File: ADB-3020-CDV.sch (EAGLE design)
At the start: 118 parts, among them IC1 7812T, IC2 NE5532N, IC3 LM2576, IC4 NE555, IC5 IR2184D, J1 + IN, J2 - IN, J3 - IN, J4 - OUT, J5 PIN2F061.040, J6 + OUT, J7 PIN2F061.040, J8 + IN, Q1 IRFP240-H, Q2 IRFP240-H, Q4 BDX53, T1 BC337, T2 BC337, X1-1 LSP13, X1-2 LSP13, X2-1 LSP13, X2-2 LSP13

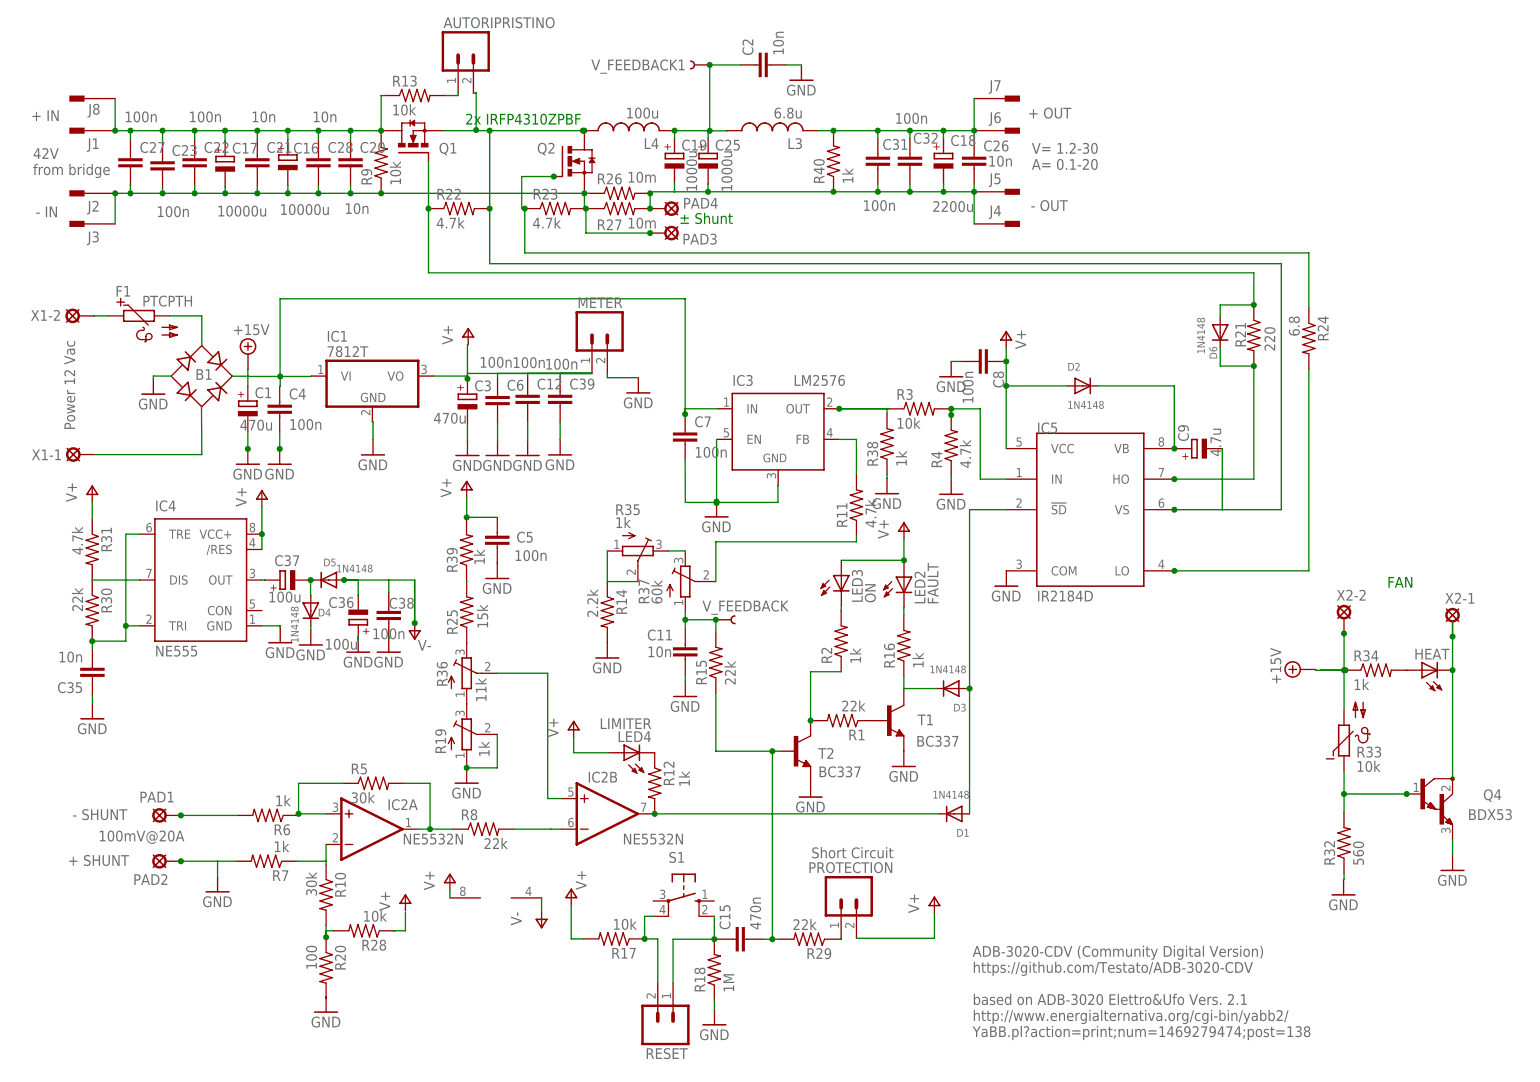
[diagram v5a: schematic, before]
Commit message: Grid 0,1" + some component name corrections
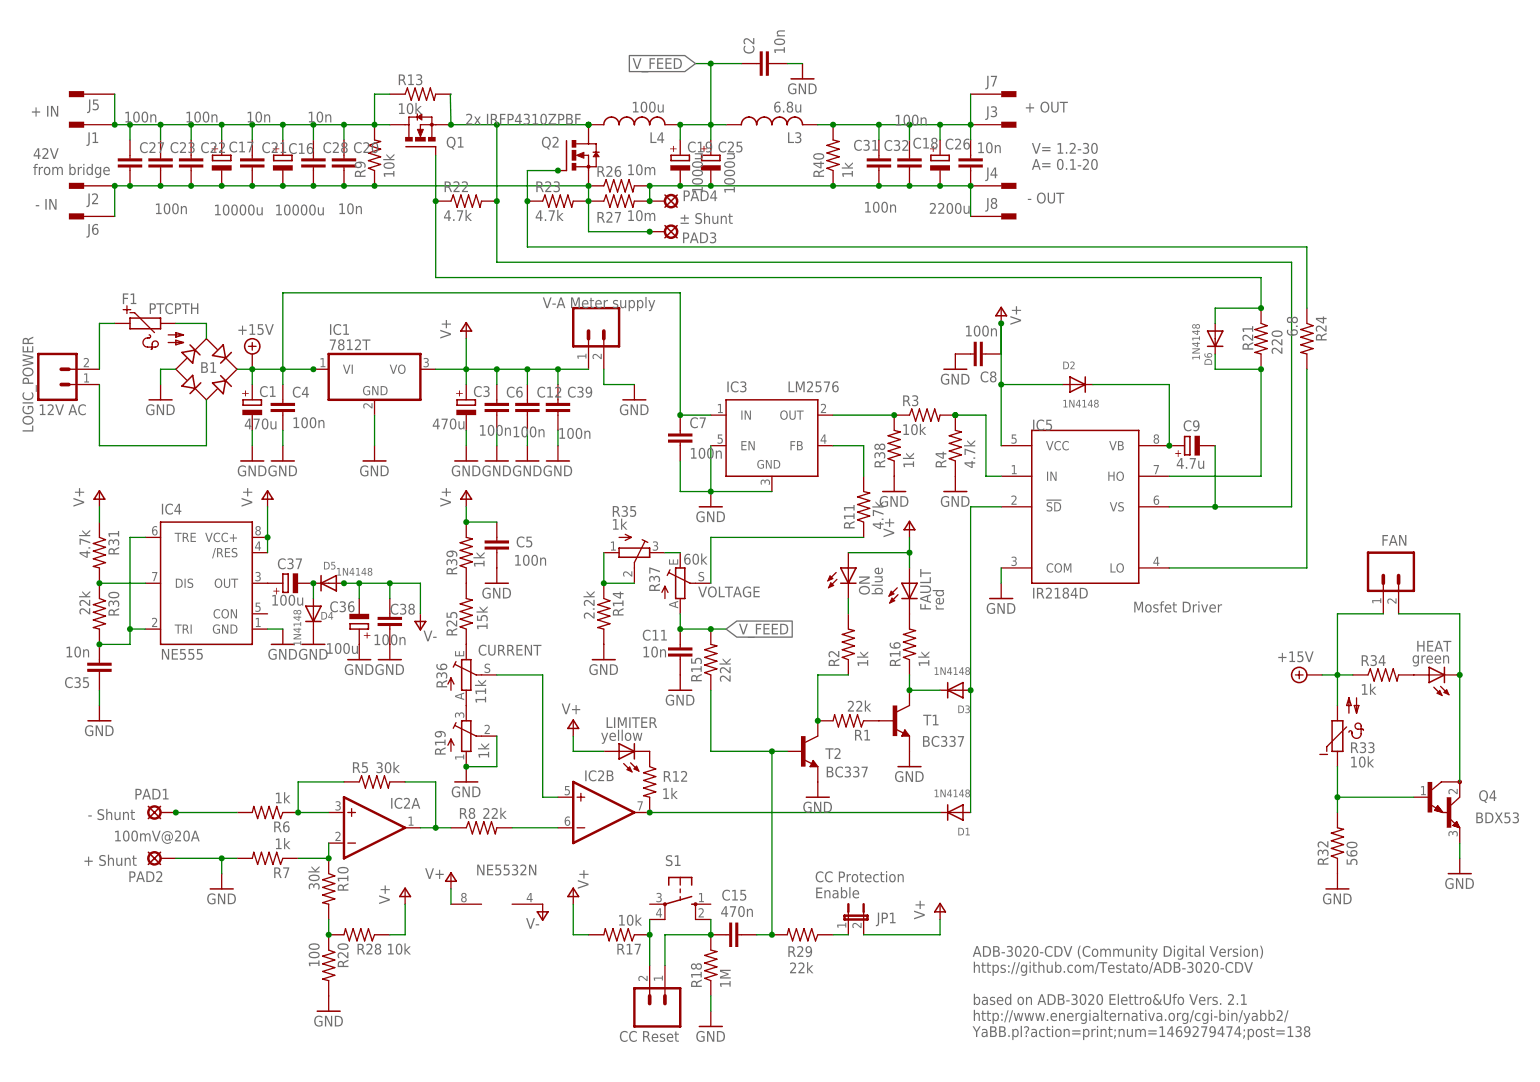
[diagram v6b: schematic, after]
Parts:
- removed AUTORIPRISTINO, METER: (no value), con-amp-quick:MA02
- removed LED2: FAULT, adafruit:LED3MM
- removed LED3: ON, adafruit:LED3MM
- removed LED4: LIMITER, adafruit:LED3MM
- removed PROTECTION: Short Circuit, con-amp-quick:MA02
- removed V_FEEDBACK, V_FEEDBACK1: MPB1, con-hirschmann:MPB1
- removed X1-1, X1-2, X2-1, X2-2: LSP13, solpad:LSP13
- added FAN: fan, con-amp-quick:MA02
- added FAULT: red, adafruit:LED3MM
- added JP1: jp1, jumper:JP1E
- added LIMITER: yellow, adafruit:LED3MM
- added LOGIC_POWER: 12V AC, con-amp-quick:MA02
- added ON: blue, adafruit:LED3MM
- added V-A_METER_SUPPLY: V-A Meter supply, con-amp-quick:MA02
- HEAT: value (none) -> green
- J3: value - IN -> + OUT
- J4: value - OUT -> PIN2F061.040
- J5: value PIN2F061.040 -> + IN
- J6: value + OUT -> - IN
- J8: value + IN -> - OUT
- R36, R37: device adafruit:TRIMPOT3386 -> pot:TRIM_1234-S64YW
- RESET, S1: value (none) -> CC Reset
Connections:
- removed net N$11: C19.+, C25.+, L4.2
- removed net N$13: PROTECTION.1, R29.1
- removed net N$16: C7.1, IC3.IN
- removed net N$17: C7.2
- removed net N$33: IC2B.-IN
- removed net N$38: R8.2
- removed net N$40: R28.1
- removed net N$49: C11.1, R15.2, R37.A, V_FEEDBACK.1
- removed net N$55: R11.2
- removed net N$72: R33.2
- removed net N$73: C2.1, L3.1, V_FEEDBACK1.1
- removed net N$8 (its old number): AUTORIPRISTINO.1, R13.2
- new net N$1: B1.AC2, LOGIC_POWER.1
- new net N$6: IC2B.-IN, R8.2
- new net V_FEED: C11.1, C19.+, C2.1, C25.+, L3.1, L4.2, R15.2, R37.A
- net +15V: now also B1.+, C1.+, C7.1, FAN.1, IC3.IN, R33.2; no longer X2-2.MP
- net GND: now also B1.-, C1.-, C4.2, C7.2, IC3.EN, IC3.GND, IC5.COM, R20.2, V-A_METER_SUPPLY.2; no longer METER.2
- net N$15: now also FAULT.C; no longer LED2.C
- net N$20: now also ON.C; no longer LED3.C
- net N$21: now also LIMITER.C; no longer LED4.C
- net N$3: now also LOGIC_POWER.2; no longer X1-2.MP
- net N$58: now also J8.1; no longer J5.1
- net N$63: now also J5.1; no longer J8.1
- net N$68: now also FAN.2; no longer X2-1.MP
- net N$7: now also IC3.FB, R11.2; no longer IC2P.V-
- net N$74: now also J6.1; no longer J3.1
- net N$77: now also J3.1; no longer J6.1
- net N$9: now also JP1.1, R29.1; no longer B1.+, C1.+
- net V+: now also FAULT.A, JP1.2, LIMITER.A, ON.A, R28.1, V-A_METER_SUPPLY.1; no longer LED2.A, LED3.A, LED4.A, METER.1, PROTECTION.2
- net V-: now also C36.-, IC2P.V-
- net VS: now also R13.2; no longer AUTORIPRISTINO.2
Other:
- note added: "+ Shunt"
- note added: "- Shunt"
- note added: "CC Protection Enable"
- note added: "CURRENT"
- note added: "Mosfet Driver"
- note added: "VOLTAGE"
- note removed: "+ SHUNT"
- note removed: "- SHUNT"
- note removed: "FAN"
- note removed: "Power 12 Vac"
- moved on the sheet: B1, C1, C11, C12, C15, C16, C17, C18, C19, C20, C21, C22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
